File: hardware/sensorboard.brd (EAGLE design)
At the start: 20.5 x 84 mm, 22 parts, among them U3 QRE1113, U4 QRE1113, U5 QRE1113, U6 QRE1113, U7 QRE1113, U8 QRE1113, U9 QRE1113

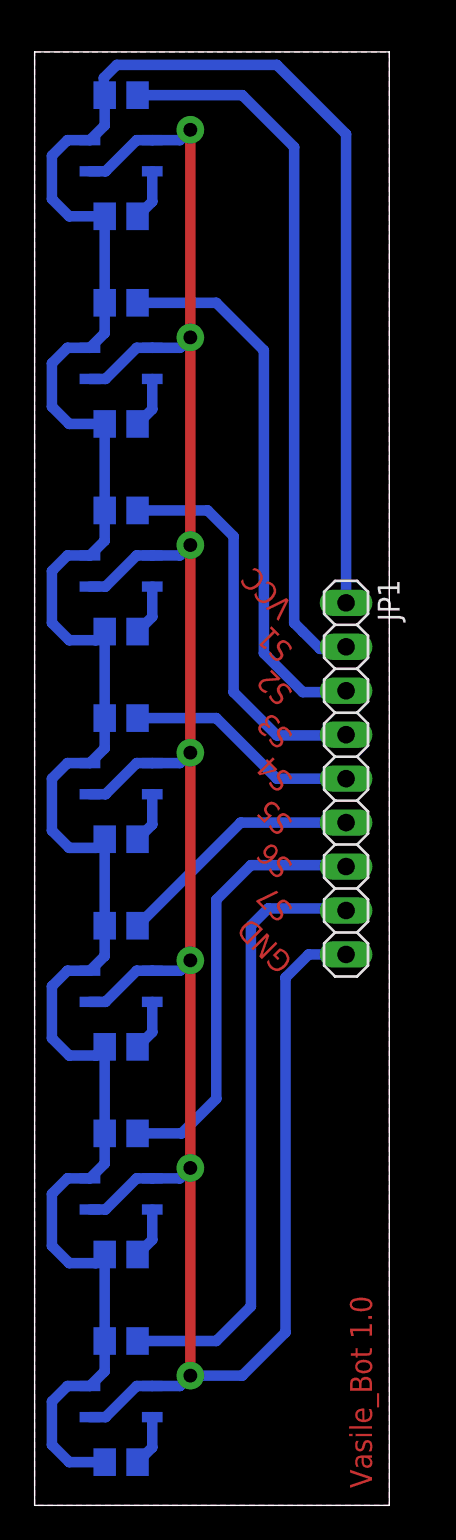
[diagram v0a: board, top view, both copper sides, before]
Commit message: Added capacitors to sensor board. Fixed routing.
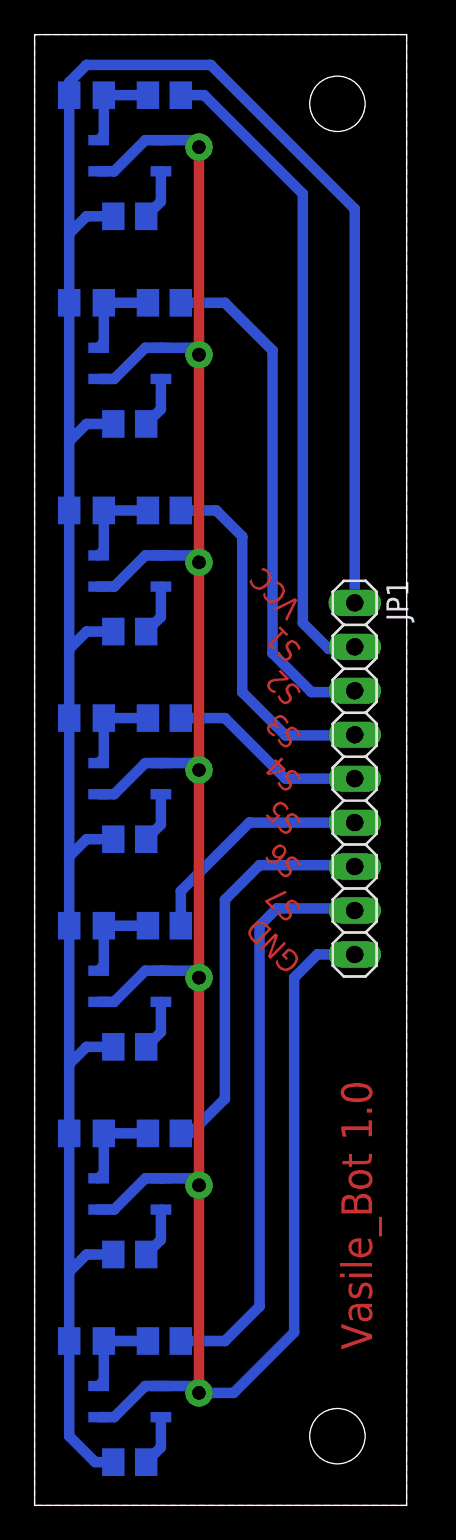
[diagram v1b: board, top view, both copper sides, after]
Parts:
- added C1, C2, C3, C4, C5, C6, C7: 10nF, resistor:C0805K
- moved R11 2.50 mm to (7.50, 33.5)
- moved R13 2.50 mm to (7.50, 21.5)
- moved R15 2.50 mm to (7.50, 45.5)
- moved R17 2.50 mm to (7.50, 57.5)
- moved R5 2.50 mm to (7.50, 81.5)
- moved R7 2.50 mm to (7.50, 69.5)
- moved R9 2.50 mm to (7.50, 9.50)
- moved JP1 0.50 mm to (18.5, 42.0)
- moved R10 0.50 mm to (5.50, 26.5)
- moved R12 0.50 mm to (5.50, 14.5)
- moved R14 0.50 mm to (5.50, 38.5)
- moved R16 0.50 mm to (5.50, 50.5)
- moved R4 0.50 mm to (5.50, 74.5)
- moved R6 0.50 mm to (5.50, 62.5)
- moved R8 0.50 mm to (5.50, 2.50)
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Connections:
- new net N$1: C1.1, R5.2, U7.3
- new net N$2: C2.1, R7.2, U3.3
- new net N$3: C3.1, R11.2, U5.3
- new net N$4: C4.1, R17.2, U9.3
- new net N$5: C7.1, R15.2, U8.3
- new net N$6: C6.1, R13.2, U6.3
- new net N$7: C5.1, R9.2, U4.3
- net VCC: now also C1.2, C2.2, C3.2, C4.2, C5.2, C6.2, C7.2; no longer R11.2, R13.2, R15.2, R17.2, R5.2, R7.2, R9.2, U3.3, U4.3, U5.3, U6.3, U7.3, U8.3, U9.3
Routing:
- net VCC: track 157.3 -> 142.3 mm
- net N$6: track 0.00 -> 5.27 mm
- net N$3: track 0.00 -> 5.27 mm
- net N$5: track 0.00 -> 5.27 mm
- net N$4: track 0.00 -> 5.27 mm
- net N$7: track 0.00 -> 5.27 mm
- net N$2: track 0.00 -> 5.27 mm
- net N$1: track 0.00 -> 5.27 mm
- net S1: track 41.5 -> 37.9 mm
- net S3: track 22.7 -> 20.7 mm
- net S2: track 31.7 -> 29.7 mm
- net S4: track 13.5 -> 11.5 mm
- net S6: track 25.2 -> 23.2 mm
- net S7: track 35.3 -> 33.3 mm
- net S5: track 14.5 -> 13.7 mm
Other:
- board size 20.5 x 84 mm -> 21.5 x 85 mm
